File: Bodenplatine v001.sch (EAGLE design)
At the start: 113 parts, among them K1 RY612012, K2 RY612012, K3 RY612012, K4 RY612012, K5 RY612012, K6 RY612012, K7 RY612012, K8 RY612012, K9 RY612012, Q1 BC846BLT1SMD, Q2 BC846BLT1SMD, Q3 BC846BLT1SMD, Q4 BC846BLT1SMD, Q5 BC846BLT1SMD, Q6 BC846BLT1SMD, Q7 BC846BLT1SMD, Q8 BC846BLT1SMD, Q9 BC846BLT1SMD, X1 SPRINGCON_AST125_5X2, X10 SPRINGCON_AST125_3X2, X11 SPRINGCON_AST125_4X2, X12 SPRINGCON_AST125_4X2, X13 SPRINGCON_AST125_5X2, X14 236-403, X15 236-402, X2 SPRINGCON_AST125_5X2, X3 SPRINGCON_AST125_5X2, X4 SPRINGCON_AST125_5X2, X5 SPRINGCON_AST125_5X2, X6 SPRINGCON_AST125_5X2, X7 SPRINGCON_AST125_5X2, X8 SPRINGCON_AST125_5X2, X9 SPRINGCON_AST125_5X2

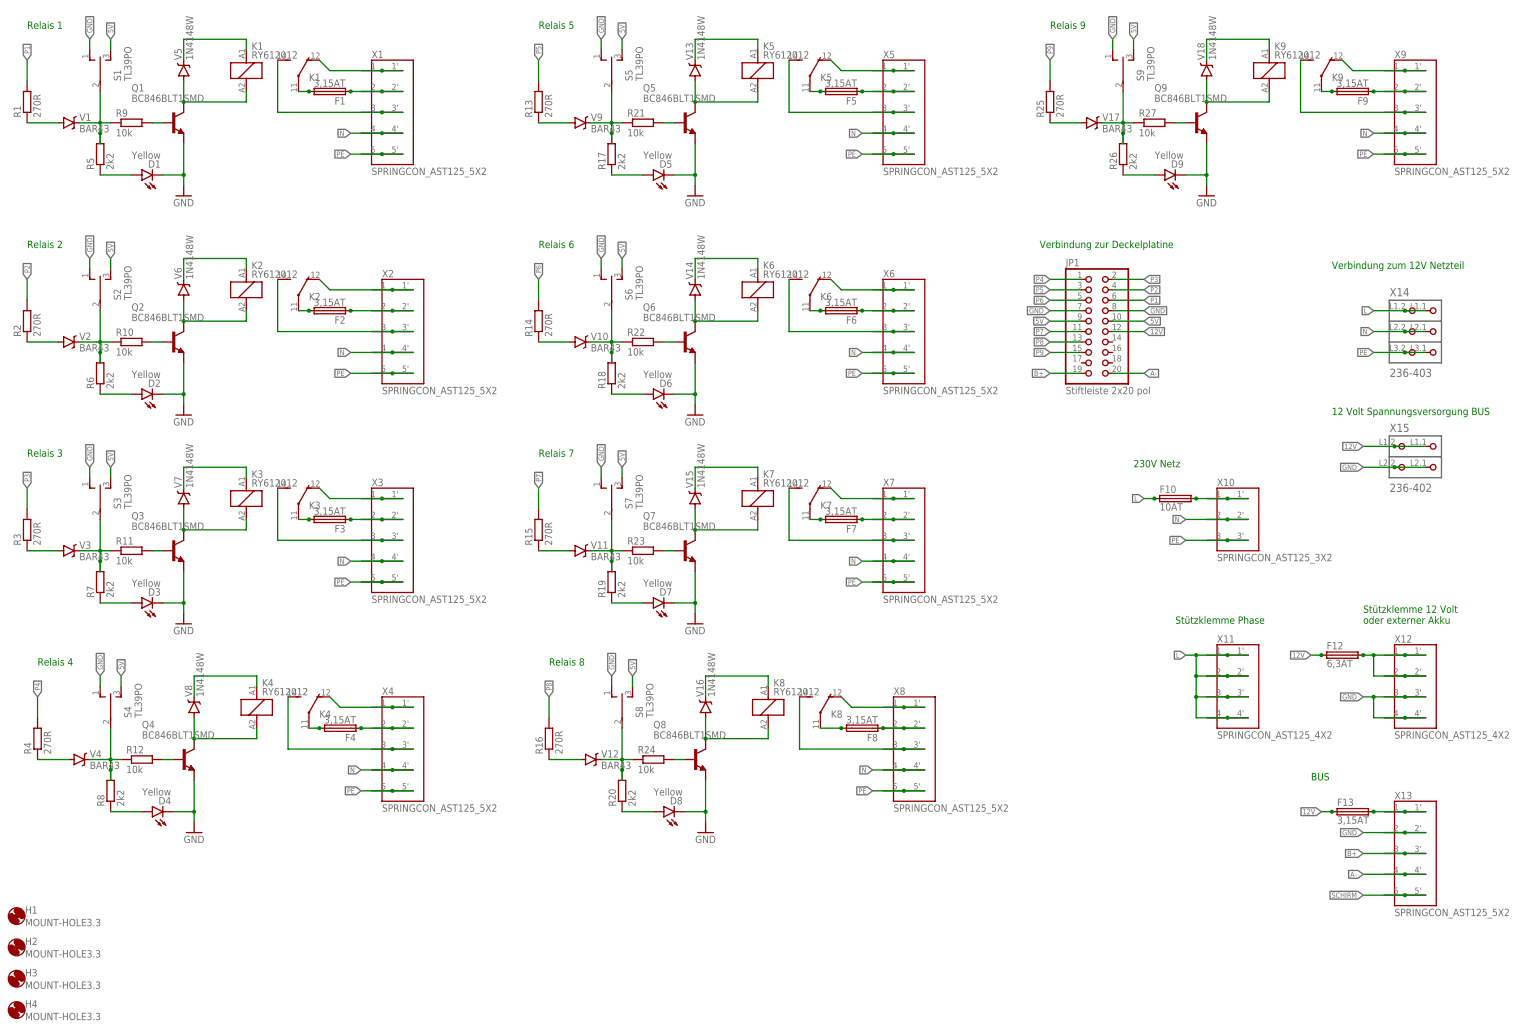
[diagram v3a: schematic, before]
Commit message: Alle Datasheets der Bodenplatine vorhanden
Auserdem noch einige Änderungen an den Footprints der Bodenplatine
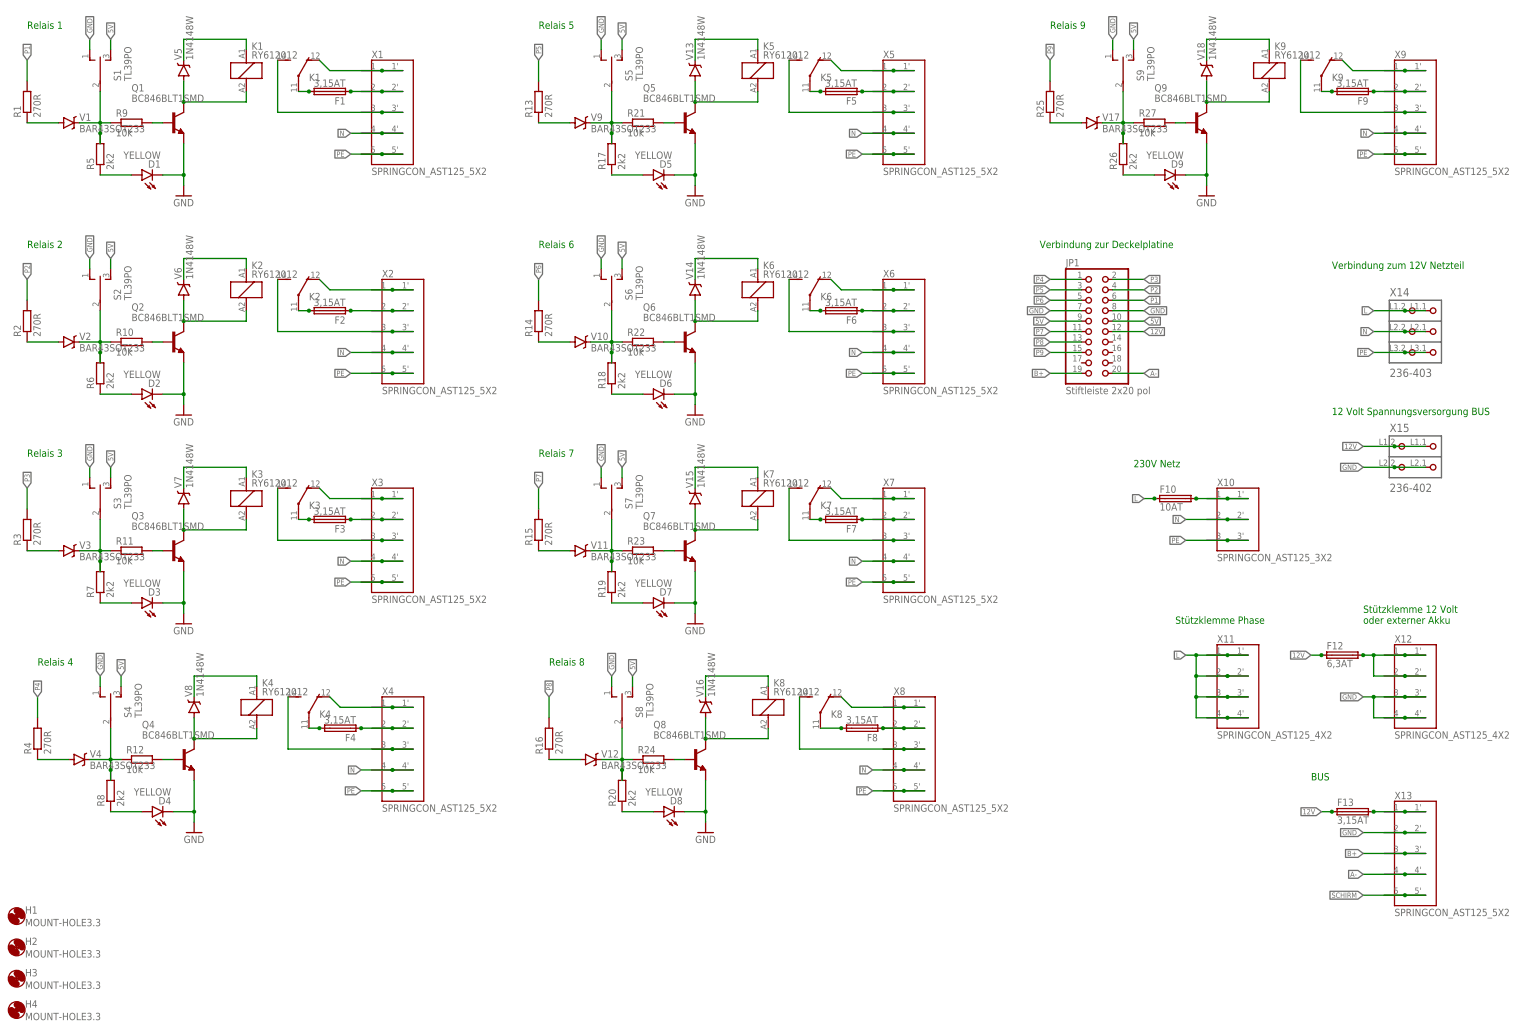
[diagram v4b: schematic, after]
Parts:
- D1, D2, D3, D4, D5, D6, D7, D8, D9: value Yellow -> YELLOW; device SparkFun-LED:LED-YELLOW0603 -> xMZ-Mod-Touch-Bodenplatine:LED-YELLOWLARGE
- V1, V10, V11, V12, V17, V2, V3, V4, V9: value BAR43 -> BAR43SOT233; device xMZ-Mod-Touch-Bodenplatine:BAR43 -> xMZ-Mod-Touch-Bodenplatine:BAR43SOT233

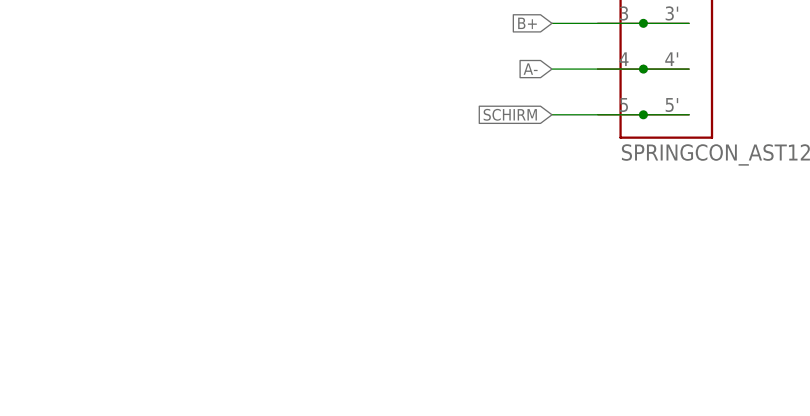
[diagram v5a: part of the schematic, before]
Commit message: Logos auch auf Schaltplan X und K Bezeichnungen auf Board verbessert
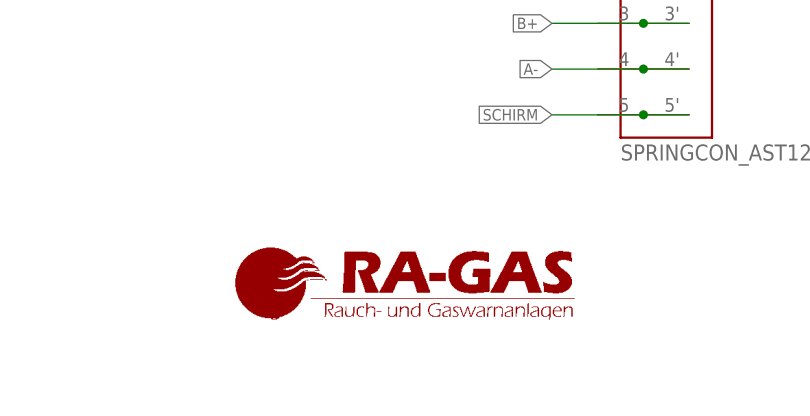
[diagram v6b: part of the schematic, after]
